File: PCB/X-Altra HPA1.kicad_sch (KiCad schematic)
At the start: 160 parts, among them J1 L_In, J2 L_In, J3 HPOut, J4 AC_In, K1 C93402, Q1 BC850C, Q10 AO3400A, Q11 BC850C, Q12 BC860C, Q2 MJE15032, Q3 MJE15033, Q4 BC850C, Q5 MJE15032, Q6 MJE15033, Q7 BC850C, Q8 BC860C, Q9 BC850C, U1 OPA1656, U2 OPA1656, U3 TL072

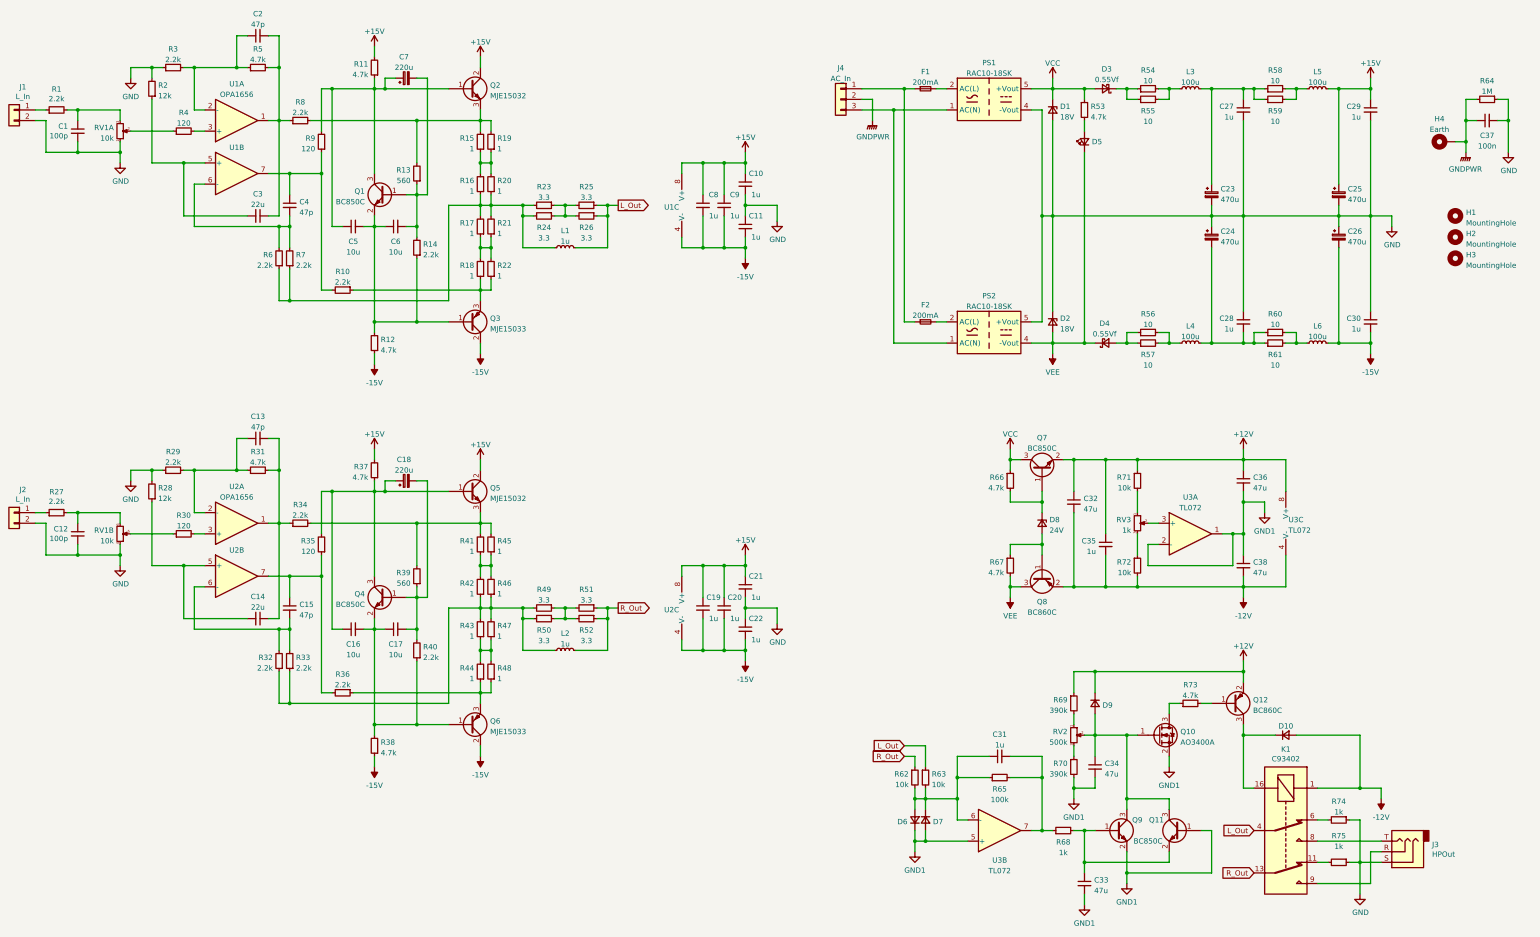
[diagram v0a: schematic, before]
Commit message: Updated resistors to 1206 for less distortion
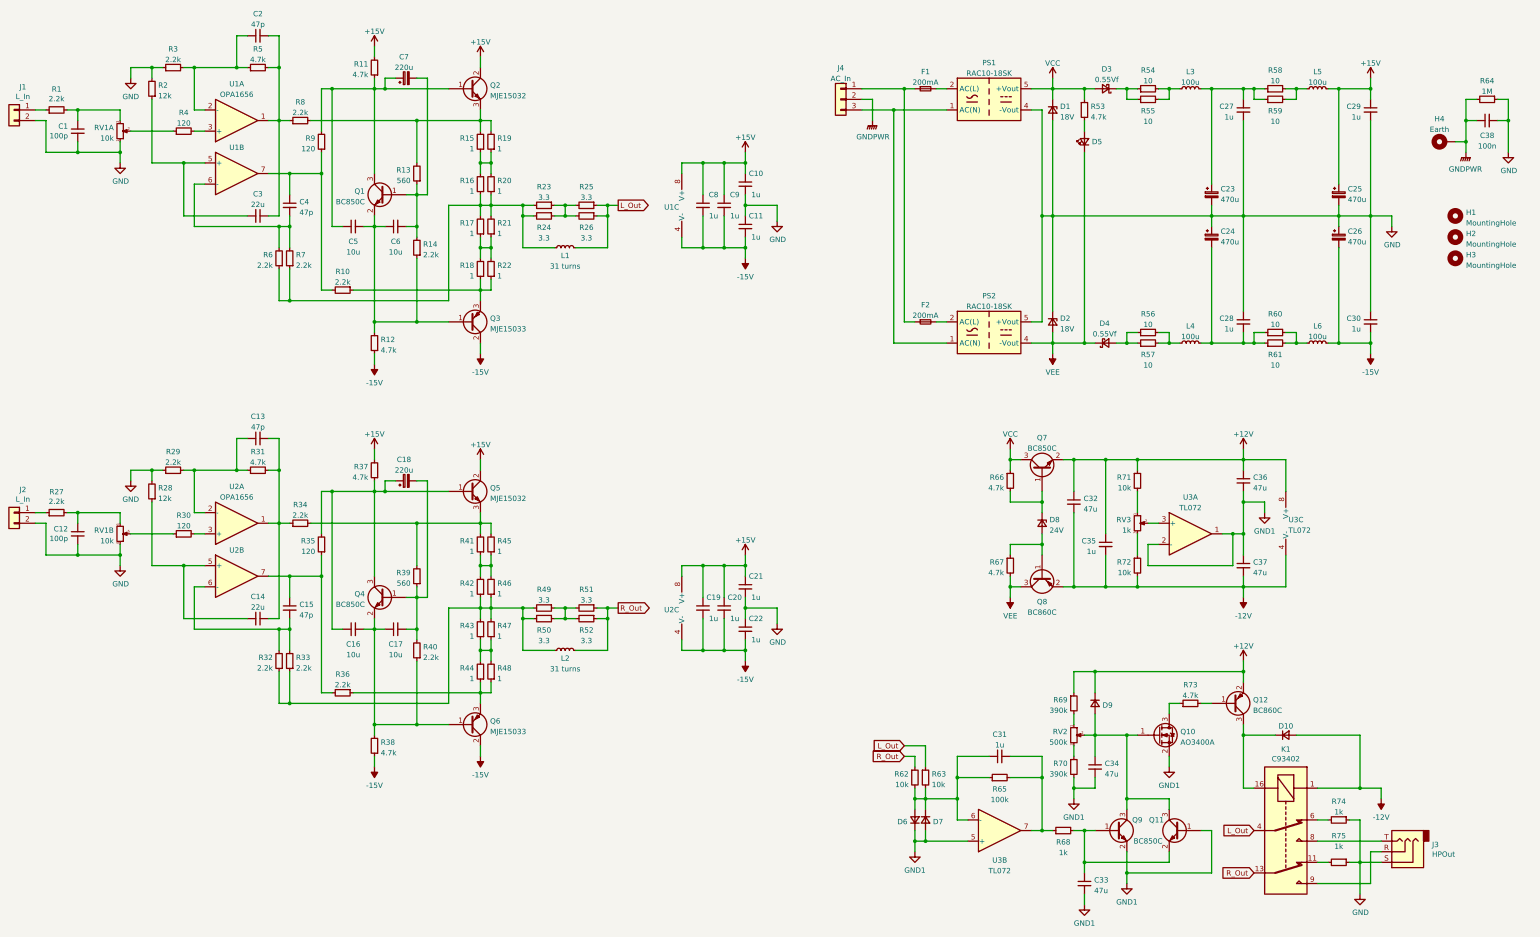
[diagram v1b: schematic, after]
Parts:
- L1, L2: value 1u -> 31 turns; footprint Inductor_THT:L_Axial_L12.0mm_D5.0mm_P15.24mm_Horizontal_Fastron_MISC -> X-Altra HPA1:L_Toroid_D15mm_W4mm; LCSC part number (none) -> N/A; Part number Hand-wound -> N/A
- R1, R10, R11, R12, R13, R14, R2, R27, R28, R29, R3, R30, R31, R32, R33, R34, R35, R36, R37, R38, R39, R4, R40, R5, R53, R6, R62, R63, R65, R66, R67, R68, R69, R7, R70, R71, R72, R73, R74, R75, R8, R9: footprint Resistor_SMD:R_0603_1608Metric -> Resistor_SMD:R_1206_3216Metric
- U1, U2, U3: footprint Package_DIP:DIP-8_W7.62mm_Socket -> Package_SO:SOIC-8_3.9x4.9mm_P1.27mm
- renumbered C38 to C37, C37 to C38

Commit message: Updated BOM
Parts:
- C32, C33, C34, C36, C37: LCSC part number C385907 -> C76659; Part number EMK316BBJ476ML-T -> C3216X5R1E476MTJ00E
- Q1, Q4: value BC850C -> BC847C; LCSC part number C80071 -> C8664; Part number BC850C,215 -> BC847C,215
- R1, R10, R14, R27, R32, R33, R34, R36, R40, R6, R7, R8: LCSC part number C706068 -> (none); Part number RT0603DRE072K2L -> RT1206BRD072K2L
- R11, R12, R31, R37, R38, R5, R53, R66, R67, R73: LCSC part number C513565 -> (none); Part number RT0603BRD074K7L -> RT1206DRD074K7L
- R13, R39: LCSC part number C861472 -> (none); Part number RT0603BRD07560RL -> RT1206BRD07560RL
- R2, R28: LCSC part number C700507 -> (none); Part number RT0603DRD0712KL -> RT1206FRE0712KL
- R23, R24, R25, R26, R49, R50, R51, R52: value 3.3 -> 3; LCSC part number C1700242 -> C326707; Part number RT1206CRD073R3L -> RT1206FRD073RL
- R29, R3: value 2.2k -> 2.7k; LCSC part number C706068 -> C870633; Part number RT0603DRE072K2L -> RT1206BRD072K7L
- R30, R35, R4, R9: value 120 -> 121; LCSC part number C861094 -> C136881; Part number RT0603BRD07120RL -> RT1206DRD07121RL
- R54, R55, R56, R57, R58, R59, R60, R61: value 10 -> 4.99; LCSC part number C870973 -> C326584; Part number RT1206BRE0710RL -> RT1206BRD074R99L
- R62, R63, R71, R72: LCSC part number C513565 -> C705072; Part number RT0603BRD074K7L -> RT1206FRD0710KL
- R64: LCSC part number C862961 -> C375528; Part number RT0603DRE071ML -> RT1206FRE071ML
- R65: LCSC part number C513565 -> C326828; Part number RT0603BRD074K7L -> RT1206FRD07100KL
- R68, R74, R75: LCSC part number C706049 -> C706405; Part number RT0603DRE071KL -> RT1206BRD071KL
- R69, R70: LCSC part number C862701 -> (none); Part number RT0603DRD07390KL -> RT1206BRD07392KL
- U3: value TL072 -> TL082; LCSC part number C110329 -> C190361; Part number TL072IP -> TL082BCDT
